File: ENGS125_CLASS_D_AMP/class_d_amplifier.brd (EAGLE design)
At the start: 89.8 x 64.8 mm, 24 parts, among them J1 BANANA_JACK_CT3151, J2 BANANA_JACK_CT3151, J3 BANANA_JACK_CT3151, J4 BANANA_JACK_CT3151, J5 BANANA_JACK_CT3151, J6 BANANA_JACK_CT3151, M1 BSC050NE2LSATMA1, M2 BSC050NE2LSATMA1, U1 LTC6992TSOT-23, U2 LTC4449

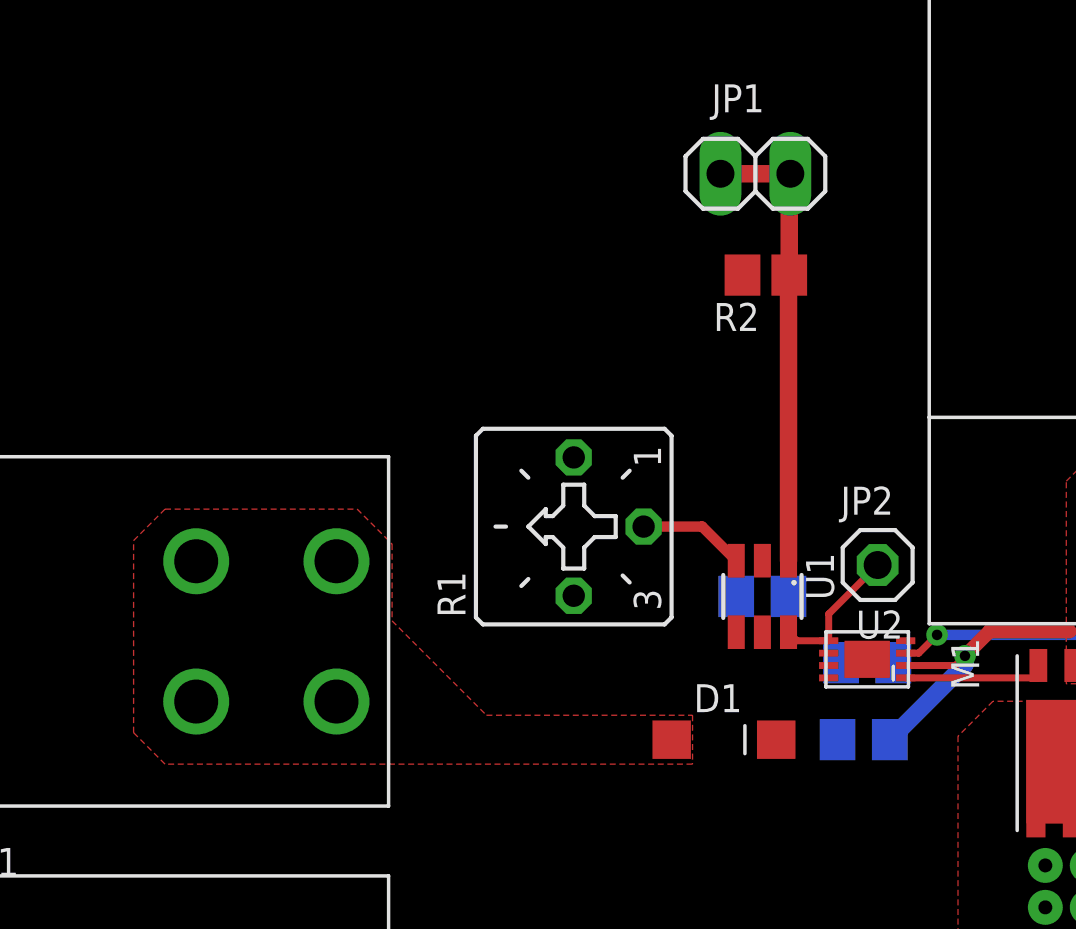
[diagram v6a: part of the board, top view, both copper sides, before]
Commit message: Began bottom layer routing for IC bypass caps
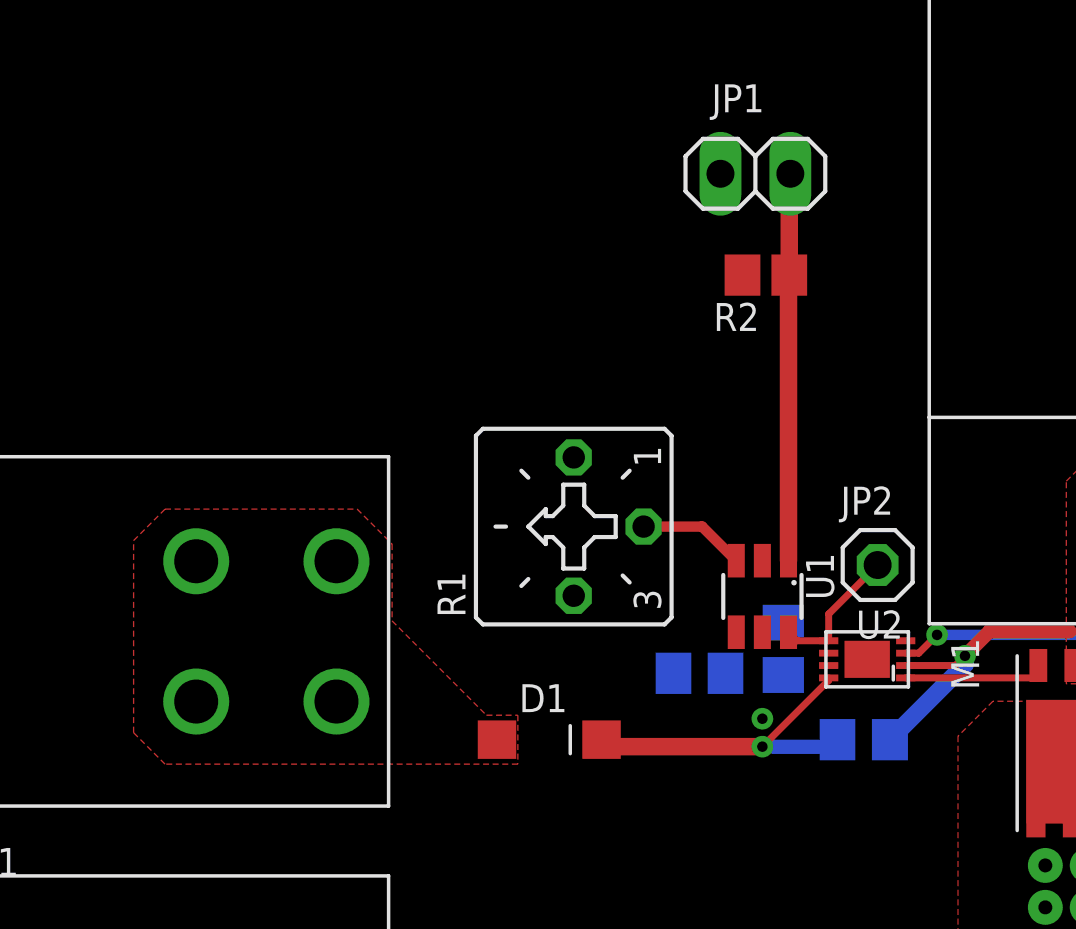
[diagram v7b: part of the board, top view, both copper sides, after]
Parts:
- moved D1 6.35 mm to (20.4, 29.1)
- moved C3 3.61 mm to (25.9, 31.5), turned to 0 degrees
- moved C4 3.09 mm to (29.0, 32.4), turned to 270 degrees
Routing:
- net N$2: track 0.00 -> 12.3 mm, vias 0 -> 1
- net N$4: track 16.6 -> 14.1 mm
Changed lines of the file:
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@@
 <attribute name="SPICEPREFIX" value="C" x="22.225" y="-15.24" size="1.778" layer="27" rot="R270" display="off"/>
 </element>
-<element name="C3" library="Engs125_library" package="C0805" value="1uF" x="28.194" y="34.29" smashed="yes" rot="MR180">
-<attribute name="NAME" x="26.924" y="33.02" size="1.016" layer="26" font="fixed" rot="MR180"/>
-</element>
-<element name="C4" library="Engs125_library" package="C0805" value="1uF" x="32.004" y="31.877" smashed="yes" rot="MR180">
-<attribute name="NAME" x="30.734" y="30.607" size="1.016" layer="26" font="fixed" rot="MR180"/>
+<element name="C3" library="Engs125_library" package="C0805" value="1uF" x="25.908" y="31.496" smashed="yes" rot="MR0">
+<attribute name="NAME" x="27.178" y="32.766" size="1.016" layer="26" font="fixed" rot="MR0"/>
+</element>
+<element name="C4" library="Engs125_library" package="C0805" value="1uF" x="28.956" y="32.385" smashed="yes" rot="MR270">
+<attribute name="NAME" x="27.686" y="33.655" size="1.016" layer="26" font="fixed" rot="MR270"/>
 </element>
 <element name="C5" library="rcl" library_urn="urn:adsk.eagle:library:334" package="C1206" package3d_urn="urn:adsk.eagle:package:23618/2" value="4.7uF" x="45.72" y="22.479" smashed="yes">
@@
 <attribute name="NAME" x="44.069" y="19.812" size="1.016" layer="25" font="fixed"/>
 </element>
-<element name="D1" library="Engs125_library" package="SOD123" value="1N5819" x="26.797" y="29.083" smashed="yes">
-<attribute name="NAME" x="25.697" y="30.083" size="1.016" layer="25" font="fixed"/>
+<element name="D1" library="Engs125_library" package="SOD123" value="1N5819" x="20.447" y="29.083" smashed="yes">
+<attribute name="NAME" x="19.347" y="30.083" size="1.016" layer="25" font="fixed"/>
 </element>
 <element name="L1" library="Engs125_library" package="SER2900" value="33u" x="48.26" y="50.8" smashed="yes">
@@
 <vertex x="0" y="0"/>
 </polygon>
-<wire x1="29.144" y1="34.29" x2="27.471" y2="45.974" width="0" layer="19" extent="1-16"/>
-<wire x1="33.404" y1="32.679" x2="32.954" y2="31.877" width="0" layer="19" extent="1-16"/>
-<wire x1="32.004" y1="32.004" x2="32.954" y2="31.877" width="0" layer="19" extent="1-16"/>
-<wire x1="27.244" y1="32.99" x2="29.144" y2="34.29" width="0" layer="19" extent="1-16"/>
+<wire x1="27.244" y1="32.99" x2="27.471" y2="45.974" width="0" layer="19" extent="1-1"/>
+<wire x1="28.956" y1="31.435" x2="27.244" y2="32.99" width="0" layer="19" extent="1-16"/>
+<wire x1="32.004" y1="32.004" x2="28.956" y2="31.435" width="0" layer="19" extent="1-16"/>
+<wire x1="33.404" y1="32.679" x2="32.004" y2="32.004" width="0" layer="19" extent="1-1"/>
 </signal>
 <signal name="VGG">
@@
 <vertex x="14.732" y="33.401"/>
 <vertex x="18.161" y="29.972"/>
-<vertex x="25.654" y="29.972"/>
-<vertex x="25.654" y="28.194"/>
+<vertex x="19.304" y="29.972"/>
+<vertex x="19.304" y="28.194"/>
 <vertex x="6.477" y="28.194"/>
 <vertex x="5.334" y="29.337"/>
 <vertex x="5.334" y="36.322"/>
 </polygon>
-<wire x1="30.604" y1="31.779" x2="31.054" y2="31.877" width="0" layer="19" extent="1-16"/>
-<wire x1="30.604" y1="32.229" x2="30.604" y2="31.779" width="0" layer="19" extent="1-1"/>
-<wire x1="28.194" y1="32.99" x2="30.604" y2="32.229" width="0" layer="19" extent="1-1"/>
-<wire x1="27.244" y1="34.29" x2="28.194" y2="32.99" width="0" layer="19" extent="1-16"/>
-<wire x1="24.897" y1="29.083" x2="28.194" y2="32.99" width="0" layer="19" extent="1-1"/>
+<via x="28.194" y="29.845" extent="1-16" drill="0.381" diameter="0.762"/>
+<wire x1="28.194" y1="32.99" x2="28.956" y2="33.335" width="0" layer="19" extent="1-16"/>
+<wire x1="30.604" y1="32.229" x2="28.956" y2="33.335" width="0" layer="19" extent="1-16"/>
+<wire x1="30.604" y1="31.779" x2="30.604" y2="32.229" width="0" layer="19" extent="1-1"/>
+<wire x1="26.858" y1="31.496" x2="28.194" y2="32.99" width="0" layer="19" extent="1-16"/>
+<wire x1="28.194" y1="29.845" x2="26.858" y2="31.496" width="0" layer="19" extent="16-16"/>
+<wire x1="18.547" y1="29.083" x2="26.858" y2="31.496" width="0" layer="19" extent="1-16"/>
 </signal>
 <signal name="VPWM">
@@
 <contactref element="U2" pad="8"/>
 <contactref element="C1" pad="1"/>
-<wire x1="30.927" y1="29.083" x2="30.604" y2="31.329" width="0" layer="19" extent="1-16"/>
-<wire x1="28.697" y1="29.083" x2="30.927" y2="29.083" width="0" layer="19" extent="1-16"/>
+<via x="28.194" y="28.829" extent="1-16" drill="0.381" diameter="0.762"/>
+<wire x1="22.347" y1="29.083" x2="22.601" y2="28.829" width="0.635" layer="1"/>
+<wire x1="22.601" y1="28.829" x2="28.194" y2="28.829" width="0.635" layer="1"/>
+<wire x1="28.194" y1="28.829" x2="30.604" y2="31.239" width="0.254" layer="1"/>
+<wire x1="30.604" y1="31.239" x2="30.604" y2="31.329" width="0.254" layer="1"/>
+<wire x1="30.927" y1="29.083" x2="30.673" y2="28.829" width="0.508" layer="16"/>
+<wire x1="30.673" y1="28.829" x2="28.194" y2="28.829" width="0.508" layer="16"/>
 </signal>
 <signal name="VSW">
@@
 <wire x1="29.171" y1="45.974" x2="29.171" y2="49.618" width="0.635" layer="1"/>
 <wire x1="29.171" y1="49.618" x2="29.21" y2="49.657" width="0.635" layer="1"/>
-<wire x1="29.21" y1="49.657" x2="26.67" y2="49.657" width="0.635" layer="1"/>
+<wire x1="29.21" y1="49.657" x2="26.67" y2="49.657" width="0" layer="19" extent="1-1"/>
 </signal>
 <signal name="N$1">
